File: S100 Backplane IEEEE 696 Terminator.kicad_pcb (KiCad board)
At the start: 2 copper layers, 56.6 x 158.8 mm, 40 parts, among them IC1 7805, IC2 LM4250, P2 BUS_IN_1, P3 BUS_IN_2, Q1 2N3906, Q2 2N3904, Q3 TIP29, Q4 TIP30

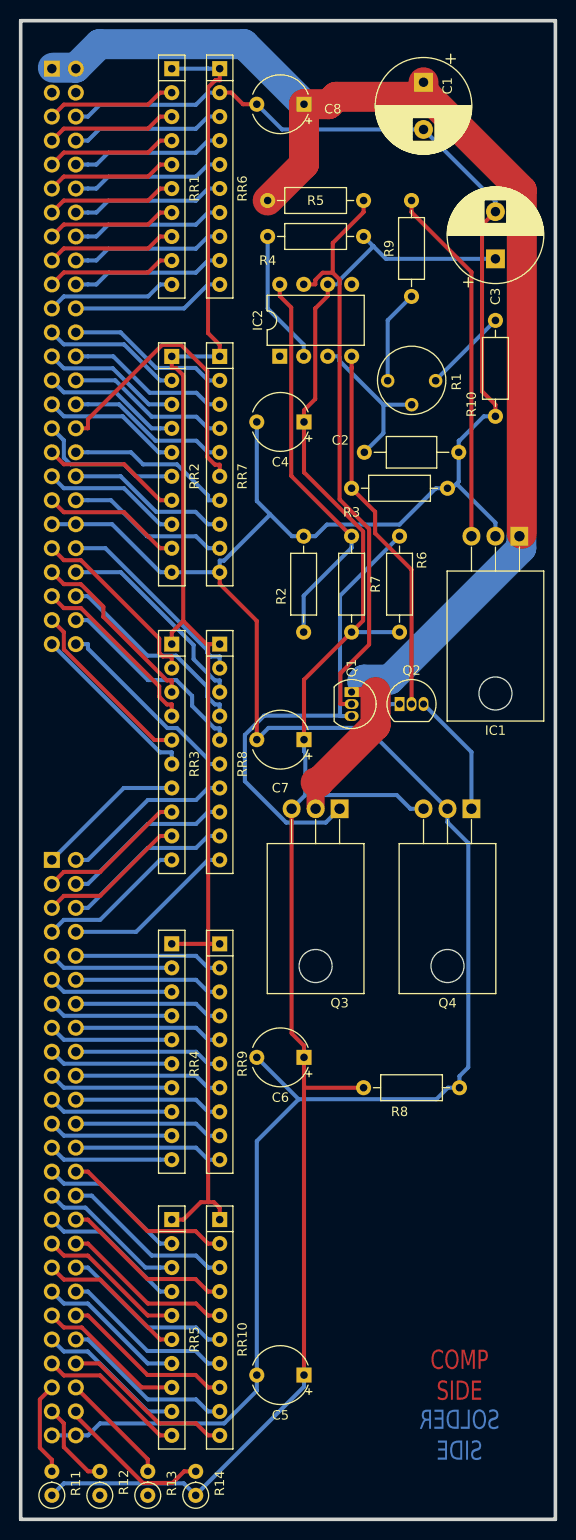
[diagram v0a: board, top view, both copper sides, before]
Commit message: Fix minor problem.
Signed-off-by: John Bradley <flypie@rocketmail.com>
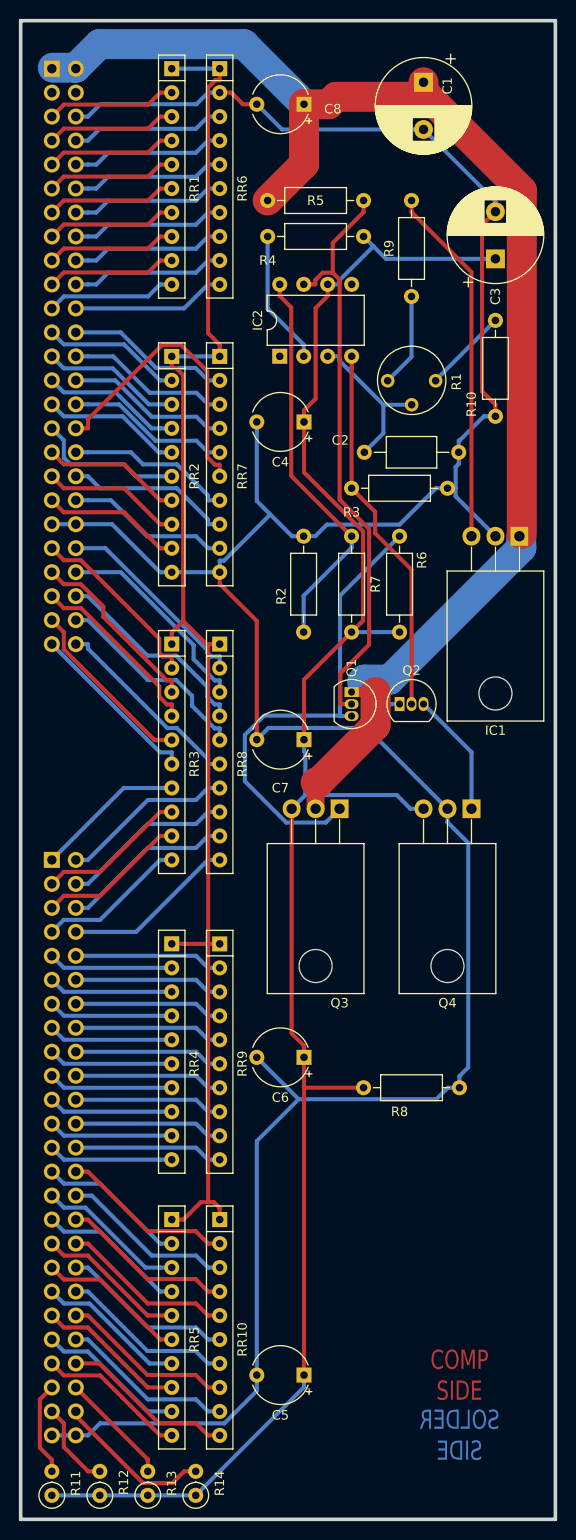
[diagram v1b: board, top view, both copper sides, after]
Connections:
- R12 pad 1: unconnected-(R12-Pad1) -> /Vacc
- R13 pad 1: unconnected-(R13-Pad1) -> /Vacc
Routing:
- net /Vacc: track 203.0 -> 201.9 mm
